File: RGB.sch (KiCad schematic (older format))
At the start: 26 parts, among them U5 74LVC1G34

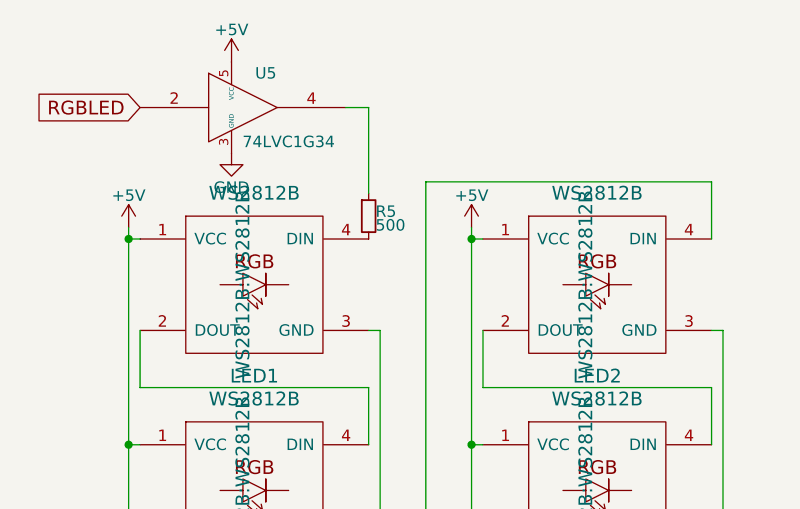
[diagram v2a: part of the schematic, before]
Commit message: Swap USB back
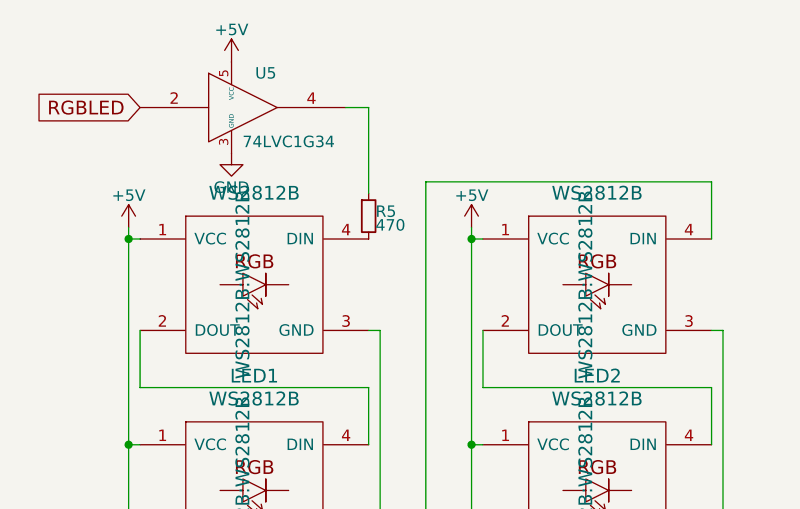
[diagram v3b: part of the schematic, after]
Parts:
- R5: value 500 -> 470
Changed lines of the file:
@@
 P 2775 1425
 F 0 "R5" H 2805 1445 50  0000 L CNN
-F 1 "500" H 2805 1385 50  0000 L CNN
+F 1 "470" H 2805 1385 50  0000 L CNN
 F 2 "Resistors_SMD:R_0603" H 2775 1425 50  0001 C CNN
 F 3 "" H 2775 1425 50  0001 C CNN

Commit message: Low cost edition complete
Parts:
- removed CRGB1, CRGB10, CRGB11, CRGB12, CRGB2, CRGB3, CRGB4, CRGB5, CRGB6, CRGB7, CRGB8, CRGB9: 0.1u, Capacitors_SMD:C_0603, symbol C_Small
- removed LED1, LED10, LED11, LED12, LED2, LED3, LED4, LED5, LED6, LED7, LED8, LED9: WS2812B, WS2812B:WS2812B, symbol WS2812B
- removed R5: 470, Resistors_SMD:R_0603, symbol R_Small
- removed U5: 74LVC1G34, TO_SOT_Packages_SMD:SOT-353_SC-70-5, symbol 74LVC1G34
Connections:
- no-connect marks 1 -> 0
